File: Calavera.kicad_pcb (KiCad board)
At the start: 2 copper layers, 39.2 x 59.2 mm, 23 parts, among them Q1 Q_DUAL_NMOS, U1 AT42QT1012, U2 LMV932

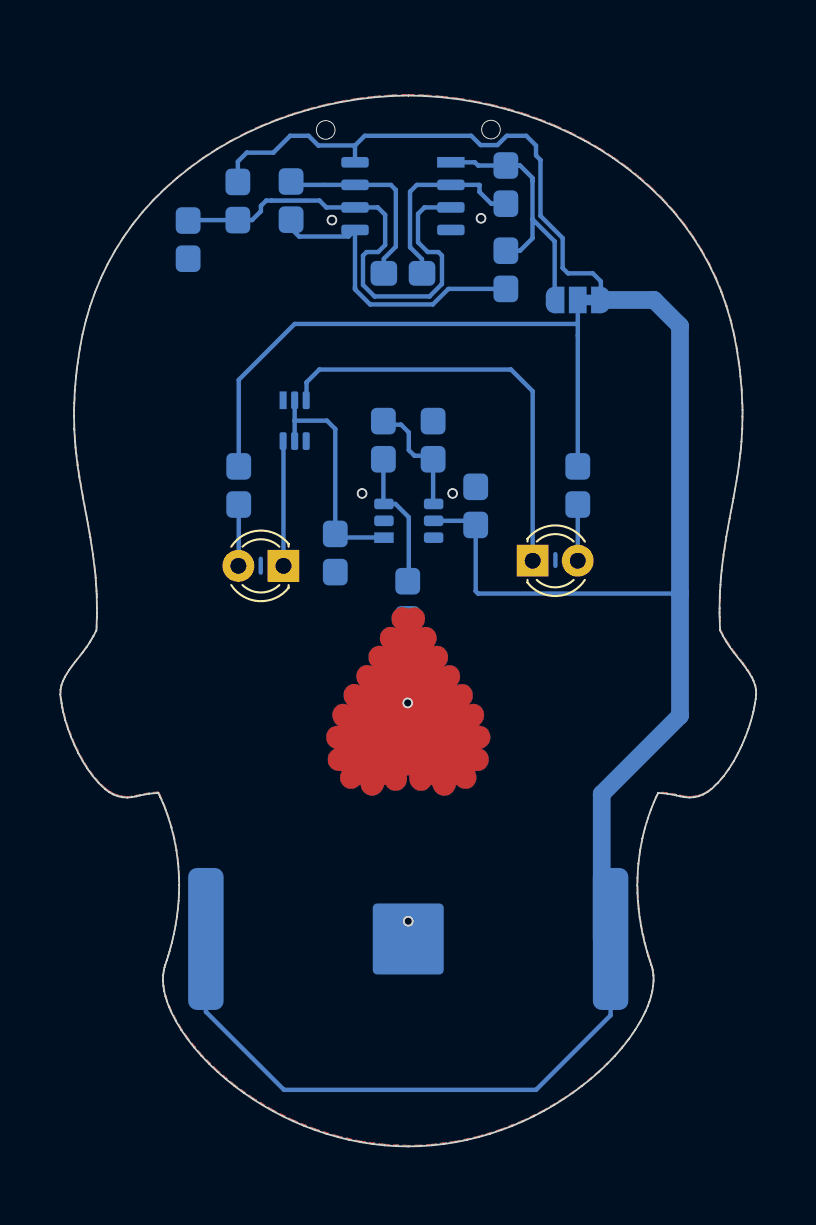
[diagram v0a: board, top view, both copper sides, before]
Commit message: Added Silk, Mask and Edge as schematic symbols Updated silk and mask, as they got misaligned Added silk to the nose pad
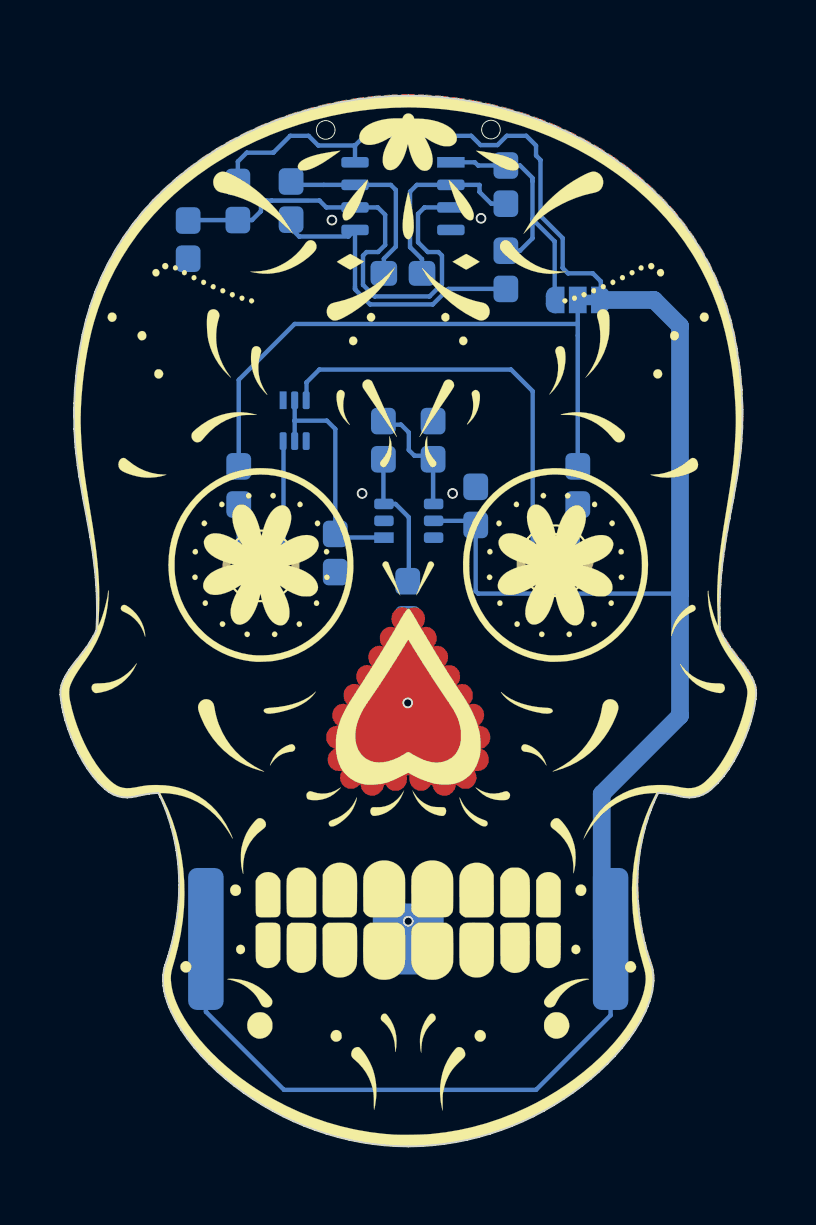
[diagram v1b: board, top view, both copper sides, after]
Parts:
- removed Margin1: Calavera_Board_Margins, Calavera:Calavera_Board_Margins
- removed Solder1: Calavera_SolderMask_1200dpi, Calavera:Calavera_SolderMask_1200dpi
- added G2: Edge, Calavera:Calavera_Board_Margins, F.Cu at (139.2, 102.8)
- added G3: Mask, Calavera:Calavera_SolderMask_1200dpi, F.Cu at (139.2, 102.8)
- added G4: Silk, Calavera:Calavera_SilkScreen_1200dpi, F.Cu at (139.2, 102.8)
- C1: value C_Small -> 22nF
- C2: value C_Small -> 100nF
- C3: value C_Small -> 22μF
- R1, R10: value R_Small_US -> 10kΩ
- R2: value R_Small_US -> 1MΩ
- R3: value R_Small_US -> 100kΩ
- R6: value R_Small_US -> 180kΩ
- R7: value R_Small_US -> 1200Ω
- R8: value R_Small_US -> 8200Ω
- R9: value R_Small_US -> 2500
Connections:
- D1 pad 1: Net-(D1-Pad1) -> VLEDK
- D2 pad 1: Net-(D2-Pad1) -> VLEDK
- Q1 pad D1: Net-(D1-Pad1) -> VLEDK
- Q1 pad D2: Net-(D2-Pad1) -> VLEDK
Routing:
- net VLEDK: track 0.00 -> 31.5 mm
- net Net-(D2-Pad1): track 24.3 -> 0.00 mm
- net Net-(D1-Pad1): track 7.27 -> 0.00 mm

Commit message: Added an exposed outline around the board (and extended the copper plane to the PCB edge) to try to get the side plated too. Changed the Silk and Soldermask parts for this change, and also corrected a small misalignment in a couple of places in the silk/mask
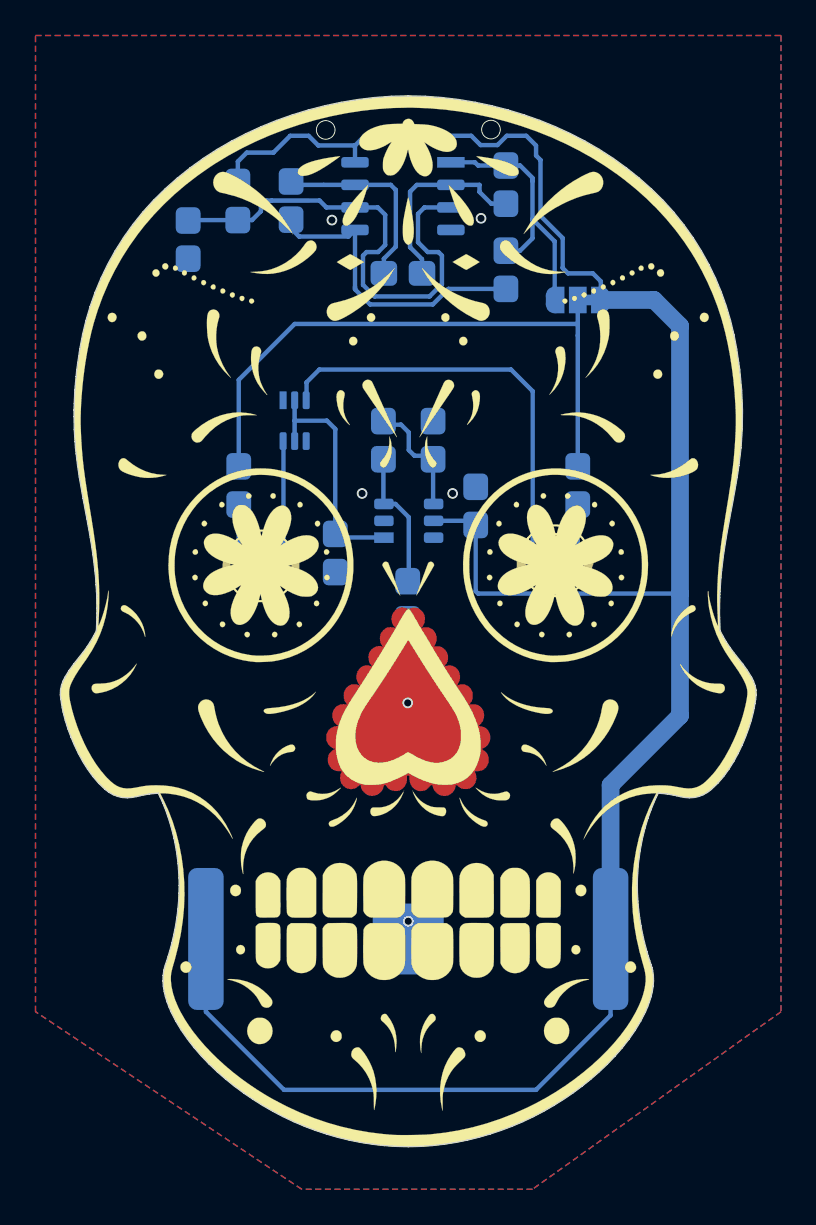
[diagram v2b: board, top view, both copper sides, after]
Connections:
- D1 pad 1: VLEDK -> VLEDK1
- D2 pad 1: VLEDK -> VLEDK2
- Q1 pad D1: VLEDK -> VLEDK1
- Q1 pad D2: VLEDK -> VLEDK2
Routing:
- net VLEDK: track 31.5 -> 0.00 mm
- net VLEDK2: track 0.00 -> 24.3 mm
- net VLEDK1: track 0.00 -> 7.27 mm

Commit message: Tweaked a couple of things on the PCB as the exposed copper on the edge of the PCB could make soldering a tad difficult
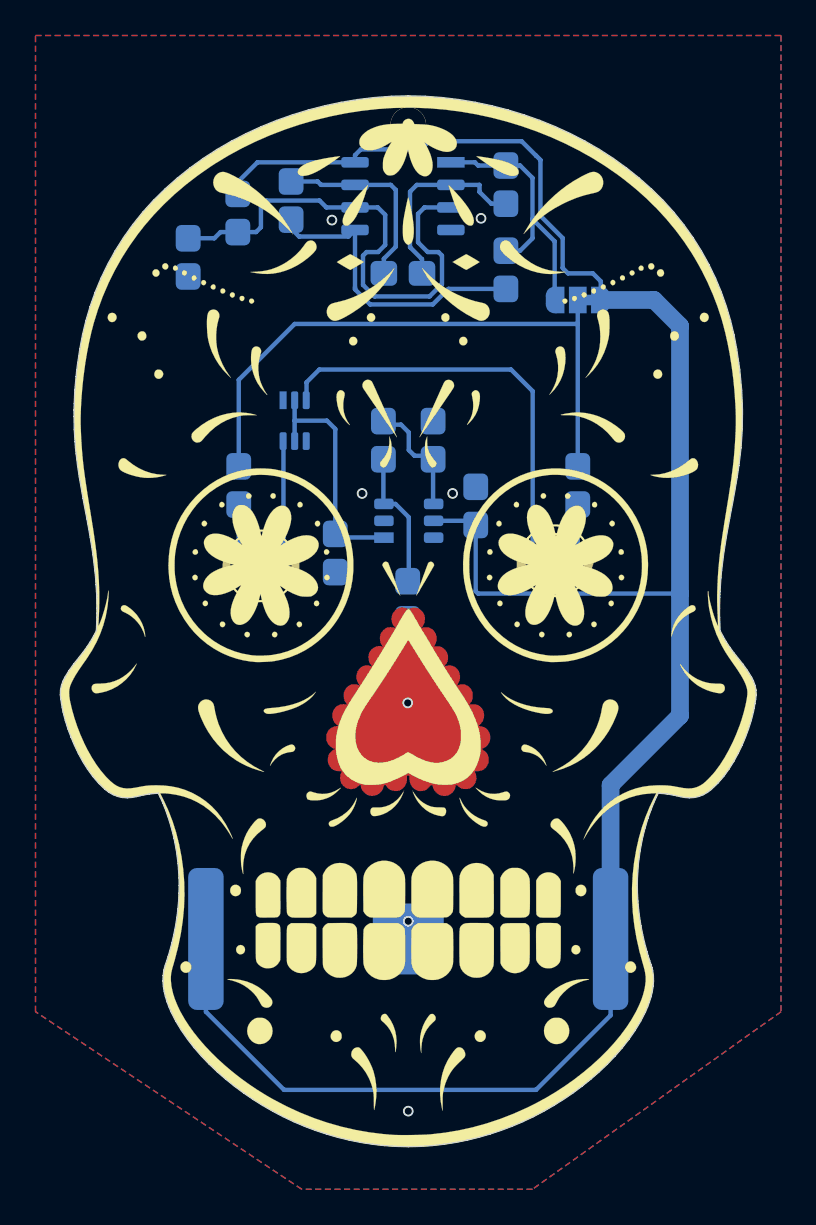
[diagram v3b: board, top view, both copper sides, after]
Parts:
- moved R10 1.00 mm to (126.8, 82.3)
- moved R9 0.67 mm to (129.6, 79.8)
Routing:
- net VCC: track 125.5 -> 123.3 mm
- net GND: track 1.44 -> 0.00 mm
- net Vbias: track 30.9 -> 29.7 mm

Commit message: Removed border plating and exposed border Sadly, it increased the cost x3!
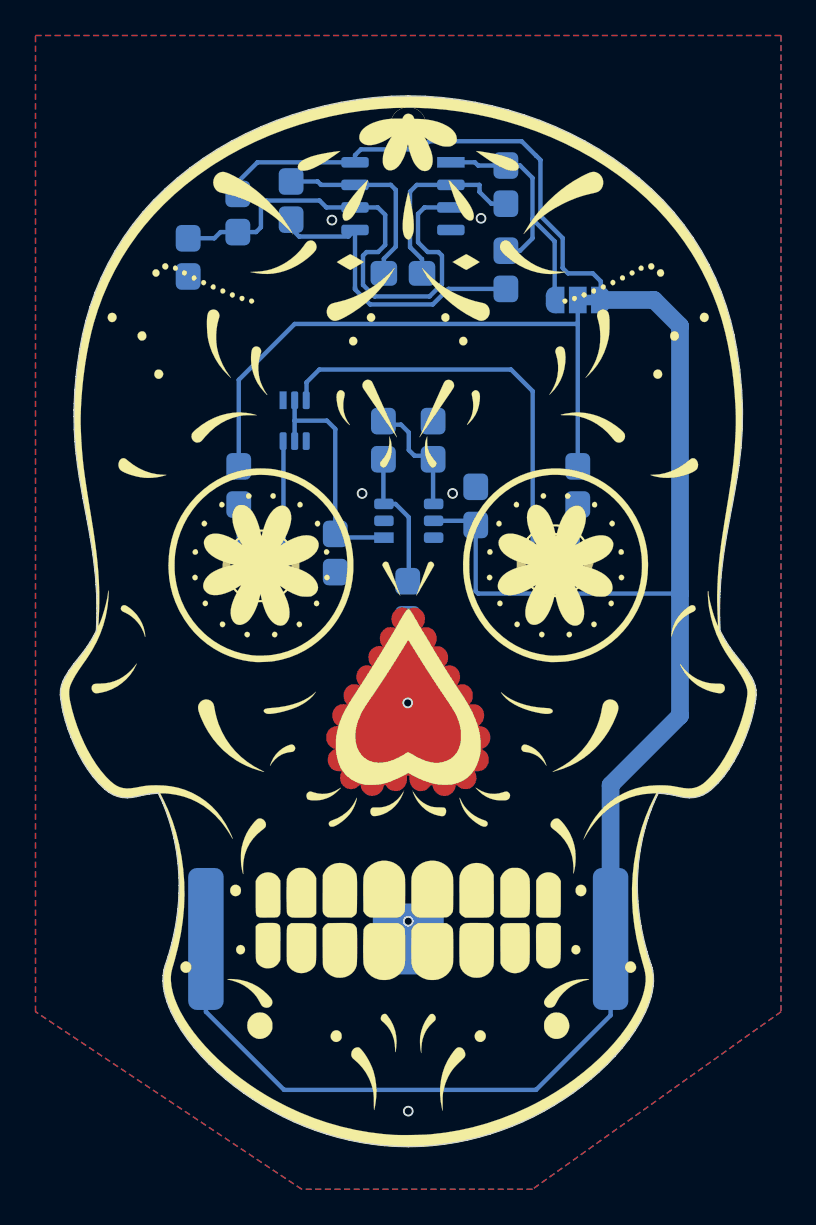
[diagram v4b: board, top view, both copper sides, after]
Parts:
- G3: footprint Calavera:Calavera_SolderMask_1200dpi -> Calavera:Calavera_SolderMask_1200dpi_No_Border

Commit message: v1.0 - Manufactured for the lunch and learn
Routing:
- net GND: vias 7 -> 10
